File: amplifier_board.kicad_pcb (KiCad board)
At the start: 2 copper layers, 87 x 63.5 mm, 81 parts, among them J1 VCC (7-14V), J2 AUDIO, J3 GND, J4 A, J5 B, J6 5V, J7 -5v, Q1 SQJ402EP, Q2 Q_NMOS_GSD, Q3 SQJ402EP, Q4 SQJ402EP, Q5 SQJ402EP, U1 AD8038, U10 LM27761, U2 AD8613, U3 LTC4444-5, U4 AD8468, U5 L7805, U7 AD8038, U8 AD8468, U9 LTC4444-5

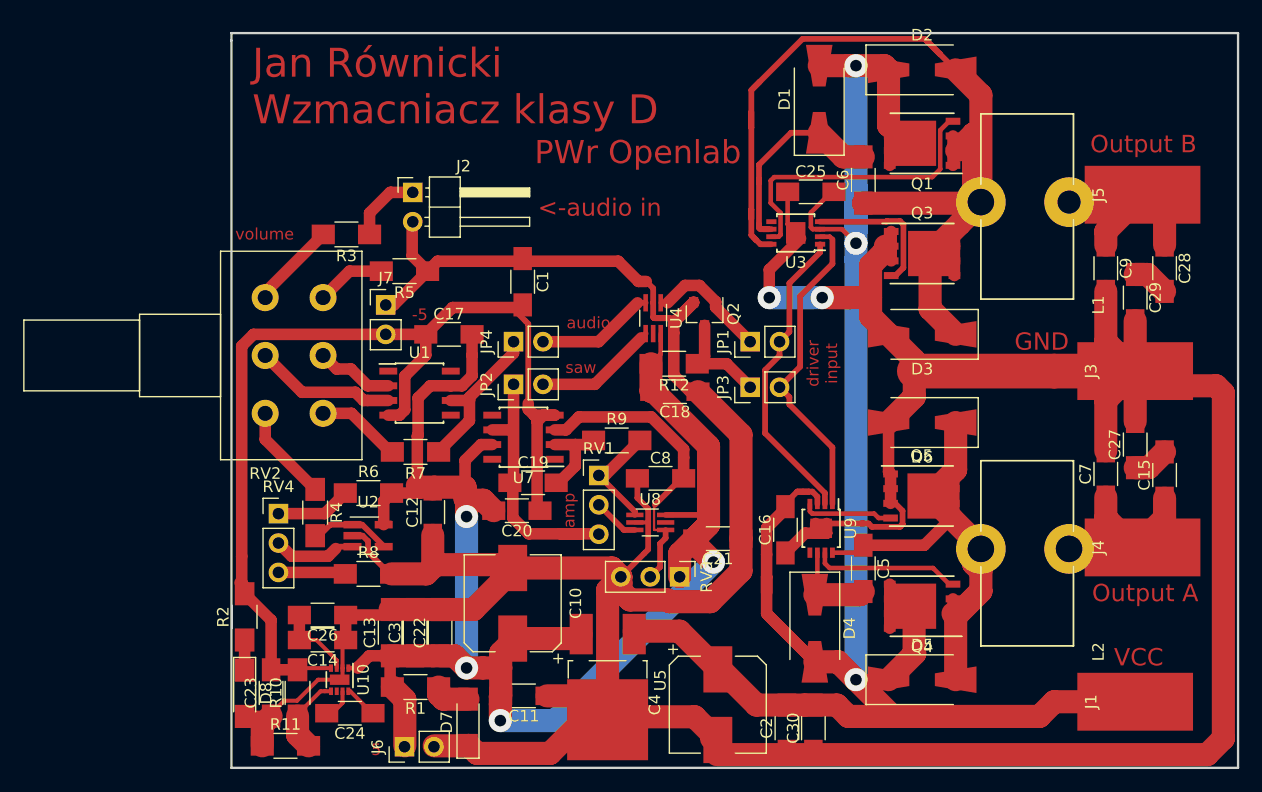
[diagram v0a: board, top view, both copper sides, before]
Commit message: updated for manufacture
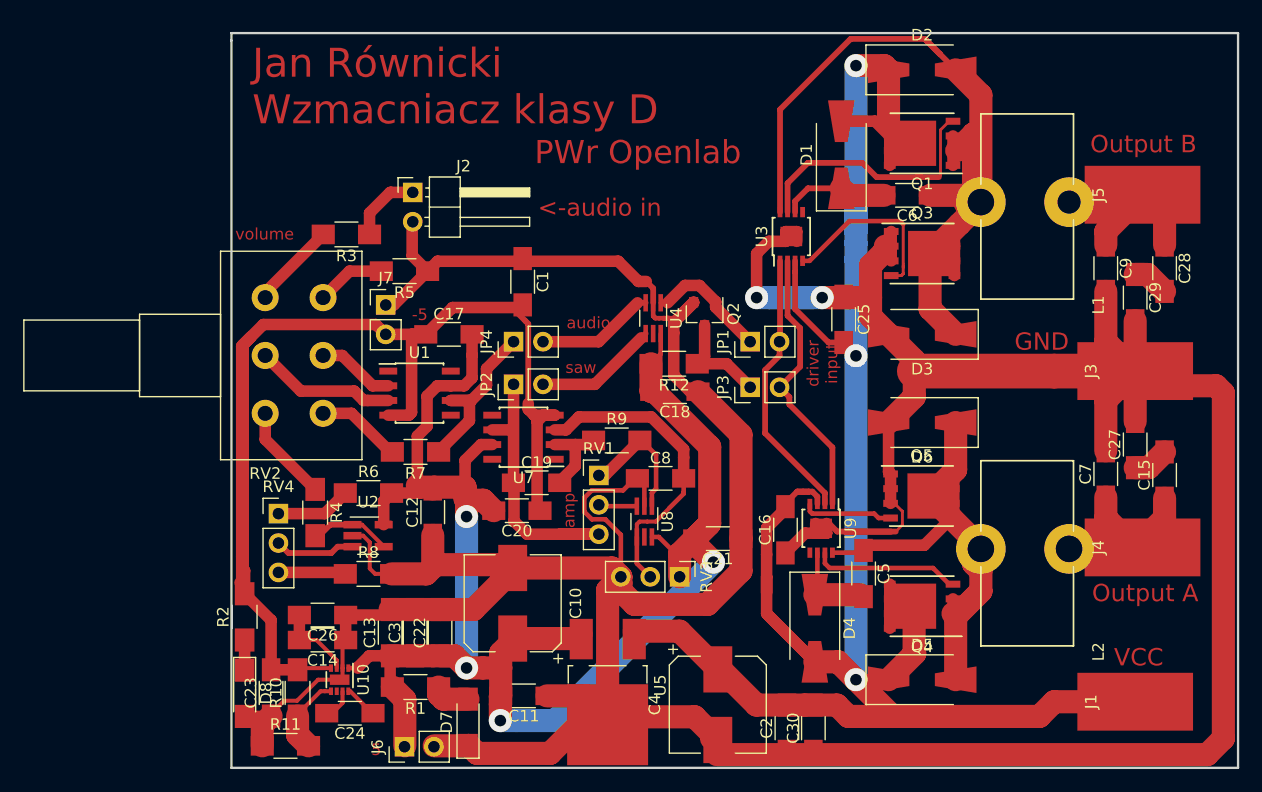
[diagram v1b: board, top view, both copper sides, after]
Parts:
- moved C25 11.4 mm to (165.3, 65.4), turned to 270 degrees
- moved D1 5.16 mm to (165.1, 51.2)
- moved C6 4.01 mm to (170.8, 54.7), turned to 180 degrees
- moved U8 0.51 mm to (148.1, 82.9), turned to 270 degrees
- moved U3 0.49 mm to (160.8, 58.2), turned to 90 degrees
- moved C5 0.44 mm to (167.0, 87.3)
- moved U5 0.43 mm to (144.9, 97.6)
- moved C19 0.30 mm to (138.8, 79.5)
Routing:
- net -5V: track 89.6 -> 134.3 mm
- net Net-(C6-Pad1): track 93.3 -> 78.3 mm
- net Net-(C6-Pad2): track 18.6 -> 9.34 mm
- net +5V: track 148.9 -> 141.9 mm
- net GND: track 419.0 -> 424.4 mm
- net Net-(JP3-Pad2): track 27.8 -> 24.1 mm
- net Net-(Q3-Pad4): track 17.4 -> 21.0 mm
- net Net-(JP1-Pad2): track 26.6 -> 23.7 mm
- net Net-(R9-Pad2): track 9.51 -> 11.3 mm
- net Net-(JP4-Pad1): track 14.4 -> 16.1 mm
- net Net-(Q1-Pad4): track 25.7 -> 24.2 mm
- net Net-(C19-Pad1): track 28.7 -> 30.2 mm
- net VCC: track 196.8 -> 197.8 mm
- net Net-(RV1-Pad2): track 4.02 -> 3.34 mm
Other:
- net class Default: clearance 0.15 -> 0.25
- rule trace_clearance: 0.15 -> 0.25
